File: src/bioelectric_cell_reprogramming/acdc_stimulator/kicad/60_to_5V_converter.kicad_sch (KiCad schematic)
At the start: 7 parts, among them IC5 LTC3637IMSE#PBF

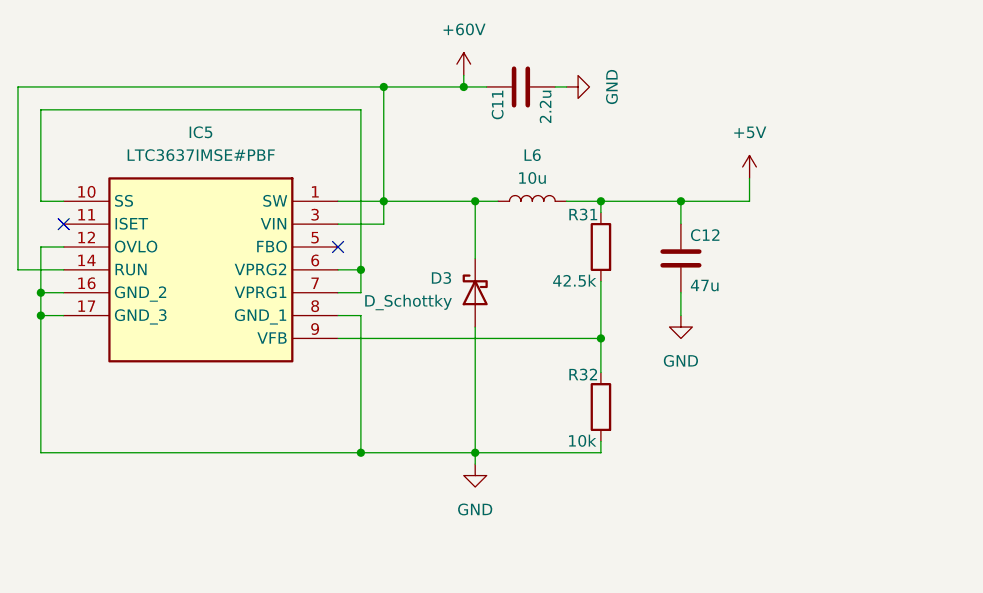
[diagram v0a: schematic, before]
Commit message: CI: footprint assignment done
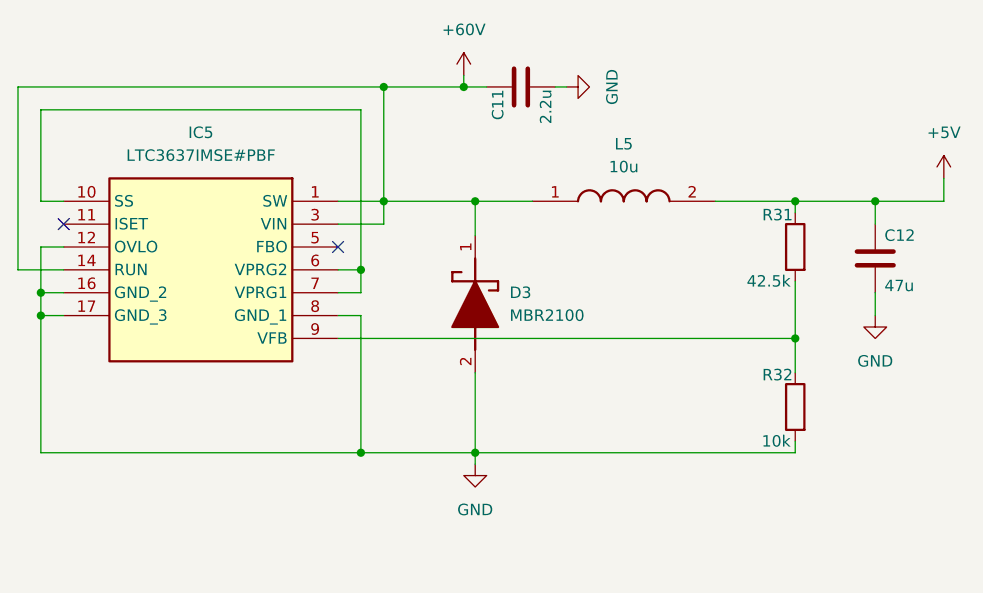
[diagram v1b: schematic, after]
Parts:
- removed D3: D_Schottky, symbol Device:D_Schottky
- removed L6: 10u, symbol Device:L
- added D3: MBR2100, MBR2100:DIOAD1910W86L670D310, symbol MBR2100:MBR2100
- added L5: 10u, SRP1270-100M:INDPM137137X700N, symbol SRP1270-100M:SRP1270-100M
- C11: footprint (none) -> Capacitor_SMD:C_0603_1608Metric
- C12: footprint (none) -> Capacitor_SMD:C_0805_2012Metric
- IC5: footprint LTC3637IMSEPBF -> LTC3637IMSE#PBF:LTC3637IMSEPBF
- R31, R32: footprint (none) -> Resistor_SMD:R_0402_1005Metric
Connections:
- net +5V: now also L5.2
- net +60V: now also D3.1 (K), L5.1
- net GND: now also D3.2 (A)
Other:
- moved on the sheet: C12, R31, R32

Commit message: ci: STM32 layout done and schematic annotated
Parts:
- renumbered C11 to C55, C12 to C56, L5 to L6, R31 to R30, R32 to R31
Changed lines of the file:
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@@
 		(dnp no)
 		(fields_autoplaced yes)
-		(property "Reference" "#PWR088"
+		(property "Reference" "#PWR093"
 			(at 219.71 86.36 0)
 			(effects
@@
 			(project "acdc_stimulator"
 				(path "/ec70e9f6-566f-44ea-8141-5580f51beca4/96d91c0a-dca3-4e1e-85a2-01b86266cb17"
-					(reference "#PWR088")
+					(reference "#PWR093")
 					(unit 1)
 				)
@@
 		(dnp no)
 		(fields_autoplaced yes)
-		(property "Reference" "#PWR087"
+		(property "Reference" "#PWR092"
 			(at 212.09 104.14 0)
 			(effects
@@
 			(project "acdc_stimulator"
 				(path "/ec70e9f6-566f-44ea-8141-5580f51beca4/96d91c0a-dca3-4e1e-85a2-01b86266cb17"
-					(reference "#PWR087")
+					(reference "#PWR092")
 					(unit 1)
 				)
@@
 		(on_board yes)
 		(dnp no)
-		(property "Reference" "C12"
+		(property "Reference" "C56"
 			(at 213.106 88.9 0)
 			(effects
@@
 			(project "acdc_stimulator"
 				(path "/ec70e9f6-566f-44ea-8141-5580f51beca4/96d91c0a-dca3-4e1e-85a2-01b86266cb17"
-					(reference "C12")
+					(reference "C56")
 					(unit 1)
 				)
@@
 		(dnp no)
 		(fields_autoplaced yes)
-		(property "Reference" "#PWR085"
+		(property "Reference" "#PWR090"
 			(at 167.64 120.65 0)
 			(effects
@@
 			(project "acdc_stimulator"
 				(path "/ec70e9f6-566f-44ea-8141-5580f51beca4/96d91c0a-dca3-4e1e-85a2-01b86266cb17"
-					(reference "#PWR085")
+					(reference "#PWR090")
 					(unit 1)
 				)
@@
 		(dnp no)
 		(fields_autoplaced yes)
-		(property "Reference" "#PWR084"
+		(property "Reference" "#PWR089"
 			(at 166.37 74.93 0)
 			(effects
@@
 			(project "acdc_stimulator"
 				(path "/ec70e9f6-566f-44ea-8141-5580f51beca4/96d91c0a-dca3-4e1e-85a2-01b86266cb17"
-					(reference "#PWR084")
+					(reference "#PWR089")
 					(unit 1)
 				)
@@
 		(dnp no)
 		(fields_autoplaced yes)
-		(property "Reference" "L5"
+		(property "Reference" "L6"
 			(at 184.15 78.74 0)
 			(effects
@@
 			(project ""
 				(path "/ec70e9f6-566f-44ea-8141-5580f51beca4/96d91c0a-dca3-4e1e-85a2-01b86266cb17"
-					(reference "L5")
+					(reference "L6")
 					(unit 1)
 				)
@@
 		(on_board yes)
 		(dnp no)
-		(property "Reference" "R32"
+		(property "Reference" "R31"
 			(at 202.946 104.394 0)
 			(effects
@@
 			(project "acdc_stimulator"
 				(path "/ec70e9f6-566f-44ea-8141-5580f51beca4/96d91c0a-dca3-4e1e-85a2-01b86266cb17"
-					(reference "R32")
+					(reference "R31")
 					(unit 1)
 				)
@@
 		(on_board yes)
 		(dnp no)
-		(property "Reference" "C11"
+		(property "Reference" "C55"
 			(at 170.18 72.644 0)
 			(effects
@@
 			(project "acdc_stimulator"
 				(path "/ec70e9f6-566f-44ea-8141-5580f51beca4/96d91c0a-dca3-4e1e-85a2-01b86266cb17"
-					(reference "C11")
+					(reference "C55")
 					(unit 1)
 				)
@@
 		(dnp no)
 		(fields_autoplaced yes)
-		(property "Reference" "#PWR086"
+		(property "Reference" "#PWR091"
 			(at 184.15 72.39 0)
 			(effects
@@
 			(project "acdc_stimulator"
 				(path "/ec70e9f6-566f-44ea-8141-5580f51beca4/96d91c0a-dca3-4e1e-85a2-01b86266cb17"
-					(reference "#PWR086")
+					(reference "#PWR091")
 					(unit 1)
 				)
@@
 		(on_board yes)
 		(dnp no)
-		(property "Reference" "R31"
+		(property "Reference" "R30"
 			(at 202.946 86.614 0)
 			(effects
@@
 			(project "acdc_stimulator"
 				(path "/ec70e9f6-566f-44ea-8141-5580f51beca4/96d91c0a-dca3-4e1e-85a2-01b86266cb17"
-					(reference "R31")
-					(unit 1)
-				)
+					(reference "R30")
+					(unit 1)
+				)

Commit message: ci: layout done
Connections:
- net +60V: no longer D3.1 (K), IC5.1 (SW), L6.1
- new net: D3.1 (K), IC5.1 (SW), L6.1
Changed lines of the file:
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@@
-	)
-	(junction
-		(at 157.48 85.09)
-		(diameter 0)
-		(color 0 0 0 0)
 	)
 	(junction
@@
 	)
 	(junction
+		(at 119.38 95.25)
+		(diameter 0)
+		(color 0 0 0 0)
+	)
+	(junction
+		(at 167.64 85.09)
+		(diameter 0)
+		(color 0 0 0 0)
+	)
+	(junction
+		(at 203.2 100.33)
+		(diameter 0)
+		(color 0 0 0 0)
+	)
+	(junction
 		(at 157.48 72.39)
-		(diameter 0)
-		(color 0 0 0 0)
-	)
-	(junction
-		(at 119.38 95.25)
-		(diameter 0)
-		(color 0 0 0 0)
-	)
-	(junction
-		(at 167.64 85.09)
-		(diameter 0)
-		(color 0 0 0 0)
-	)
-	(junction
-		(at 203.2 100.33)
 		(diameter 0)
 		(color 0 0 0 0)
@@
 	(wire
 		(pts
-			(xy 157.48 85.09) (xy 152.4 85.09)
+			(xy 152.4 85.09) (xy 167.64 85.09)
 		)
 		(stroke
@@
 	(wire
 		(pts
-			(xy 157.48 85.09) (xy 167.64 85.09)
-		)
-		(stroke
-			(width 0)
-			(type default)
-		)
-	)
-	(wire
-		(pts
 			(xy 154.94 92.71) (xy 154.94 95.25)
 		)
@@
 	(wire
 		(pts
-			(xy 157.48 72.39) (xy 157.48 85.09)
-		)
-		(stroke
-			(width 0)
-			(type default)
-		)
-	)
-	(wire
-		(pts
 			(xy 116.84 72.39) (xy 157.48 72.39)
 		)
@@
 	(wire
 		(pts
+			(xy 157.48 72.39) (xy 166.37 72.39)
+		)
+		(stroke
+			(width 0)
+			(type default)
+		)
+	)
+	(wire
+		(pts
 			(xy 203.2 111.76) (xy 203.2 113.03)
 		)
@@
 	(wire
 		(pts
-			(xy 166.37 72.39) (xy 157.48 72.39)
-		)
-		(stroke
-			(width 0)
-			(type default)
-		)
-	)
-	(wire
-		(pts
 			(xy 121.92 92.71) (xy 116.84 92.71)
 		)
@@
 	(wire
 		(pts
-			(xy 157.48 85.09) (xy 157.48 87.63)
-		)
-		(stroke
+			(xy 157.48 72.39) (xy 157.48 87.63)
+		)
+		(stroke

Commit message: fixed some more clearance errors
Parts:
- R31: Distributor Link (none) -> https://jlcpcb.com/partdetail/259901-NQ02WGJ0103TCE/C270371; Manufacturer (none) -> UNI-ROYAL(Uniroyal Elec); Manufacturer Part Number (none) -> NQ02WGJ0103TCE
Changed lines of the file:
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@@
+			)
+		)
+		(property "Distributor Link" ""
+			(at 167.64 86.36 0)
+			(effects
+				(font
+					(size 1.27 1.27)
+				)
+				(hide yes)
+			)
+		)
+		(property "Manufacturer" ""
+			(at 167.64 86.36 0)
+			(effects
+				(font
+					(size 1.27 1.27)
+				)
+				(hide yes)
+			)
+		)
+		(property "Manufacturer Part Number" ""
+			(at 167.64 86.36 0)
+			(effects
+				(font
+					(size 1.27 1.27)
+				)
+				(hide yes)
 			)
 		)
@@
 			)
 		)
+		(property "Distributor Link" ""
+			(at 152.4 85.09 0)
+			(effects
+				(font
+					(size 1.27 1.27)
+				)
+				(hide yes)
+			)
+		)
+		(property "Manufacturer" ""
+			(at 152.4 85.09 0)
+			(effects
+				(font
+					(size 1.27 1.27)
+				)
+				(hide yes)
+			)
+		)
+		(property "Manufacturer Part Number" ""
+			(at 152.4 85.09 0)
+			(effects
+				(font
+					(size 1.27 1.27)
+				)
+				(hide yes)
+			)
+		)
 		(pin "14"
 		)
@@
 		)
 		(property "Description" "Unpolarized capacitor"
+			(at 212.09 91.44 0)
+			(effects
+				(font
+					(size 1.27 1.27)
+				)
+				(hide yes)
+			)
+		)
+		(property "Distributor Link" ""
+			(at 212.09 91.44 0)
+			(effects
+				(font
+					(size 1.27 1.27)
+				)
+				(hide yes)
+			)
+		)
+		(property "Manufacturer" ""
+			(at 212.09 91.44 0)
+			(effects
+				(font
+					(size 1.27 1.27)
+				)
+				(hide yes)
+			)
+		)
+		(property "Manufacturer Part Number" ""
 			(at 212.09 91.44 0)
 			(effects
@@
 			)
 		)
+		(property "Distributor Link" ""
+			(at 173.99 85.09 0)
+			(effects
+				(font
+					(size 1.27 1.27)
+				)
+				(hide yes)
+			)
+		)
+		(property "Manufacturer" ""
+			(at 173.99 85.09 0)
+			(effects
+				(font
+					(size 1.27 1.27)
+				)
+				(hide yes)
+			)
+		)
+		(property "Manufacturer Part Number" ""
+			(at 173.99 85.09 0)
+			(effects
+				(font
+					(size 1.27 1.27)
+				)
+				(hide yes)
+			)
+		)
 		(pin "2"
 		)
@@
 			)
 		)
+		(property "Distributor Link" "https://jlcpcb.com/partdetail/259901-NQ02WGJ0103TCE/C270371"
+			(at 203.2 107.95 0)
+			(effects
+				(font
+					(size 1.27 1.27)
+				)
+				(hide yes)
+			)
+		)
+		(property "Manufacturer" "UNI-ROYAL(Uniroyal Elec)"
+			(at 203.2 107.95 0)
+			(effects
+				(font
+					(size 1.27 1.27)
+				)
+				(hide yes)
+			)
+		)
+		(property "Manufacturer Part Number" "NQ02WGJ0103TCE"
+			(at 203.2 107.95 0)
+			(effects
+				(font
+					(size 1.27 1.27)
+				)
+				(hide yes)
+			)
+		)
 		(pin "1"
 		)
@@
 		)
 		(property "Description" "Unpolarized capacitor"
+			(at 172.72 72.39 0)
+			(effects
+				(font
+					(size 1.27 1.27)
+				)
+				(hide yes)
+			)
+		)
+		(property "Distributor Link" ""
+			(at 172.72 72.39 0)
+			(effects
+				(font
+					(size 1.27 1.27)
+				)
+				(hide yes)
+			)
+		)
+		(property "Manufacturer" ""
+			(at 172.72 72.39 0)
+			(effects
+				(font
+					(size 1.27 1.27)
+				)
+				(hide yes)
+			)
+		)
+		(property "Manufacturer Part Number" ""
 			(at 172.72 72.39 0)
 			(effects
@@
 			(at 203.2 90.17 0)
 			(effects
+				(font
+					(size 1.27 1.27)
+				)
+				(hide yes)
+			)
+		)
+		(property "Distributor Link" ""
+			(at 203.2 90.17 0)
+			(effects
+				(font
+					(size 1.27 1.27)
+				)
+				(hide yes)
+			)
+		)
+		(property "Manufacturer" ""
+			(at 203.2 90.17 0)
+			(effects
+				(font
+					(size 1.27 1.27)
+				)
+				(hide yes)
+			)
+		)
+		(property "Manufacturer Part Number" ""
+			(at 203.2 90.17 0)
+			(effects

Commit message: BOM in progress
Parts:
- C55: Distributor Link (none) -> https://jlcpcb.com/partdetail/3409988-GRM21BD72A225KE01L/C2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; Manufacturer (none) -> Murata Electronics; Manufacturer Part Number (none) -> GRM21BD72A225KE01L
- C56: footprint Capacitor_SMD:C_0805_2012Metric -> Capacitor_SMD:C_1206_3216Metric; Distributor Link (none) -> https://jlcpcb.com/partdetail/183737-1206X476M160NT/C172351; Manufacturer (none) -> FH (Guangdong Fenghua Advanced Tech); Manufacturer Part Number (none) -> 1206X476M160NT
- D3: Distributor Link (none) -> https://www.digikey.com/en/products/detail/panjit-internati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; Manufacturer (none) -> Panjit International Inc.; Manufacturer Part Number (none) -> MBR2100_R2_00001
- IC5: Distributor Link (none) -> https://jlcpcb.com/partdetail/AnalogDevices-LTC3637IMSEPBF/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; Manufacturer (none) -> Analog Devices; Manufacturer Part Number (none) -> LTC3637IMSE#PBF
- L6: Distributor Link (none) -> https://www.mouser.com/ProductDetail/Bourns/SRP1270-100M?qs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; Manufacturer (none) -> Bourns; Manufacturer Part Number (none) -> SRP1270-100M
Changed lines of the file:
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@@
 			)
 		)
-		(property "Distributor Link" ""
+		(property "Distributor Link" "https://www.digikey.com/en/products/detail/panjit-international-inc/MBR2100-R2-00001/15801106"
 			(at 167.64 86.36 0)
 			(effects
@@
 			)
 		)
-		(property "Manufacturer" ""
+		(property "Manufacturer" "Panjit International Inc."
 			(at 167.64 86.36 0)
 			(effects
@@
 			)
 		)
-		(property "Manufacturer Part Number" ""
+		(property "Manufacturer Part Number" "MBR2100_R2_00001"
+			(at 167.64 86.36 0)
+			(effects
+				(font
+					(size 1.27 1.27)
+				)
+				(hide yes)
+			)
+		)
+		(property "JLCPCB Part #" ""
 			(at 167.64 86.36 0)
 			(effects
@@
 			)
 		)
-		(property "Distributor Link" ""
+		(property "Distributor Link" "https://jlcpcb.com/partdetail/AnalogDevices-LTC3637IMSEPBF/C580783"
 			(at 152.4 85.09 0)
 			(effects
@@
 			)
 		)
-		(property "Manufacturer" ""
+		(property "Manufacturer" "Analog Devices"
 			(at 152.4 85.09 0)
 			(effects
@@
 			)
 		)
-		(property "Manufacturer Part Number" ""
+		(property "Manufacturer Part Number" "LTC3637IMSE#PBF"
+			(at 152.4 85.09 0)
+			(effects
+				(font
+					(size 1.27 1.27)
+				)
+				(hide yes)
+			)
+		)
+		(property "JLCPCB Part #" ""
 			(at 152.4 85.09 0)
 			(effects
@@
 			)
 		)
-		(property "Footprint" "Capacitor_SMD:C_0805_2012Metric"
+		(property "Footprint" "Capacitor_SMD:C_1206_3216Metric"
 			(at 213.0552 95.25 0)
 			(effects
@@
 			)
 		)
-		(property "Distributor Link" ""
+		(property "Distributor Link" "https://jlcpcb.com/partdetail/183737-1206X476M160NT/C172351"
 			(at 212.09 91.44 0)
 			(effects
@@
 			)
 		)
-		(property "Manufacturer" ""
+		(property "Manufacturer" "FH (Guangdong Fenghua Advanced Tech)"
 			(at 212.09 91.44 0)
 			(effects
@@
 			)
 		)
-		(property "Manufacturer Part Number" ""
+		(property "Manufacturer Part Number" "1206X476M160NT"
+			(at 212.09 91.44 0)
+			(effects
+				(font
+					(size 1.27 1.27)
+				)
+				(hide yes)
+			)
+		)
+		(property "JLCPCB Part #" ""
 			(at 212.09 91.44 0)
 			(effects
@@
 			)
 		)
-		(property "Distributor Link" ""
+		(property "Distributor Link" "https://www.mouser.com/ProductDetail/Bourns/SRP1270-100M?qs=s%252BX%2FYkvGCpE5rFNaoMUDIw%3D%3D"
 			(at 173.99 85.09 0)
 			(effects
@@
 			)
 		)
-		(property "Manufacturer" ""
+		(property "Manufacturer" "Bourns"
 			(at 173.99 85.09 0)
 			(effects
@@
 			)
 		)
-		(property "Manufacturer Part Number" ""
+		(property "Manufacturer Part Number" "SRP1270-100M"
+			(at 173.99 85.09 0)
+			(effects
+				(font
+					(size 1.27 1.27)
+				)
+				(hide yes)
+			)
+		)
+		(property "JLCPCB Part #" ""
 			(at 173.99 85.09 0)
 			(effects
@@
 			)
 		)
+		(property "JLCPCB Part #" ""
+			(at 203.2 107.95 0)
+			(effects
+				(font
+					(size 1.27 1.27)
+				)
+				(hide yes)
+			)
+		)
 		(pin "1"
 		)
@@
 			)
 		)
-		(property "Distributor Link" ""
+		(property "Distributor Link" "https://jlcpcb.com/partdetail/3409988-GRM21BD72A225KE01L/C2981733"
 			(at 172.72 72.39 0)
 			(effects
@@
 			)
 		)
-		(property "Manufacturer" ""
+		(property "Manufacturer" " Murata Electronics"
 			(at 172.72 72.39 0)
 			(effects
@@
 			)
 		)
-		(property "Manufacturer Part Number" ""
+		(property "Manufacturer Part Number" "GRM21BD72A225KE01L"
+			(at 172.72 72.39 0)
+			(effects
+				(font
+					(size 1.27 1.27)
+				)
+				(hide yes)
+			)
+		)
+		(property "JLCPCB Part #" ""
 			(at 172.72 72.39 0)
 			(effects
@@
 			(at 203.2 90.17 0)
 			(effects
+				(font
+					(size 1.27 1.27)
+				)
+				(hide yes)
+			)
+		)
+		(property "JLCPCB Part #" ""
+			(at 203.2 90.17 0)
+			(effects

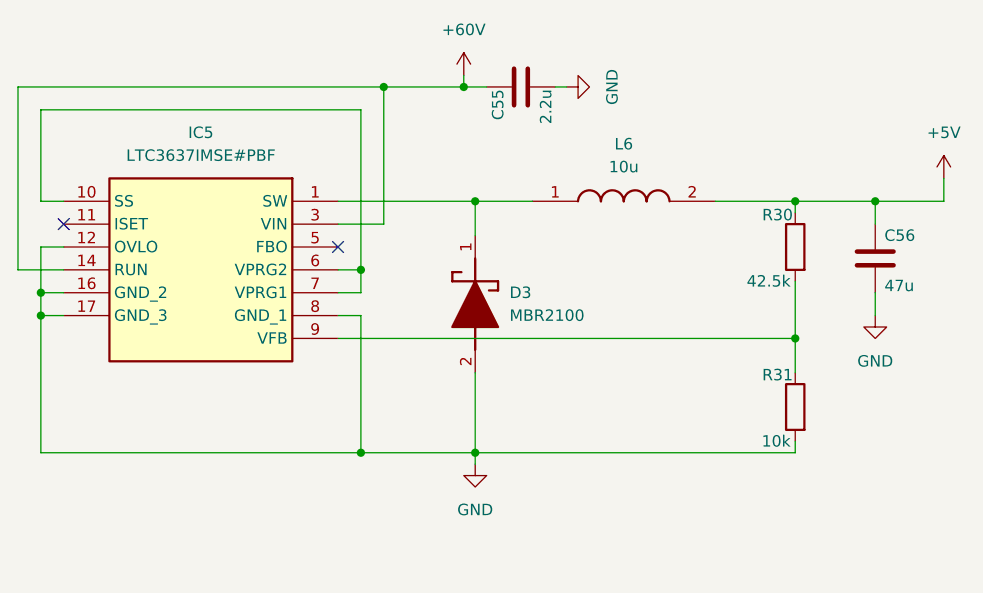
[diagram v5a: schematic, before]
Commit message: fixed values for resistive divider of LDOs
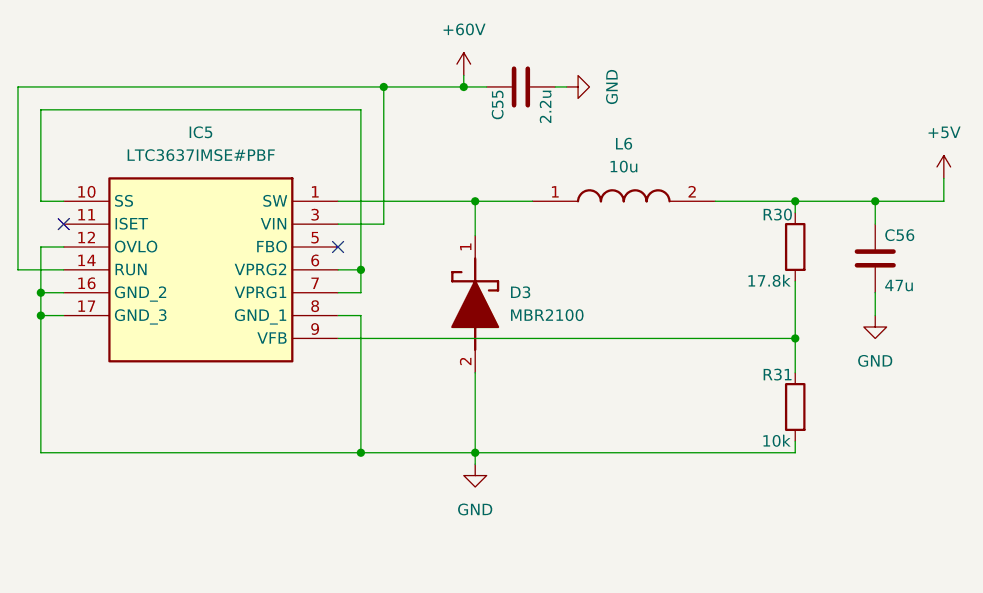
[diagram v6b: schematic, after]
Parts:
- L6: Distributor Link https://www.mouser.com/ProductDetail/Bourns/SRP1270-100M?qs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 -> https://jlcpcb.com/partdetail/Bourns-SRP1270100M/C2042024; Manufacturer Bourns -> BOURNS
- R30: value 42.5k -> 17.8k
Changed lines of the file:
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@@
 			)
 		)
-		(property "Distributor Link" "https://www.mouser.com/ProductDetail/Bourns/SRP1270-100M?qs=s%252BX%2FYkvGCpE5rFNaoMUDIw%3D%3D"
+		(property "Distributor Link" "https://jlcpcb.com/partdetail/Bourns-SRP1270100M/C2042024"
 			(at 173.99 85.09 0)
 			(effects
@@
 			)
 		)
-		(property "Manufacturer" "Bourns"
+		(property "Manufacturer" "BOURNS"
 			(at 173.99 85.09 0)
 			(effects
@@
 			)
 		)
-		(property "Value" "42.5k"
+		(property "Value" "17.8k"
 			(at 202.692 93.98 0)
 			(effects

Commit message: ci: BOM done
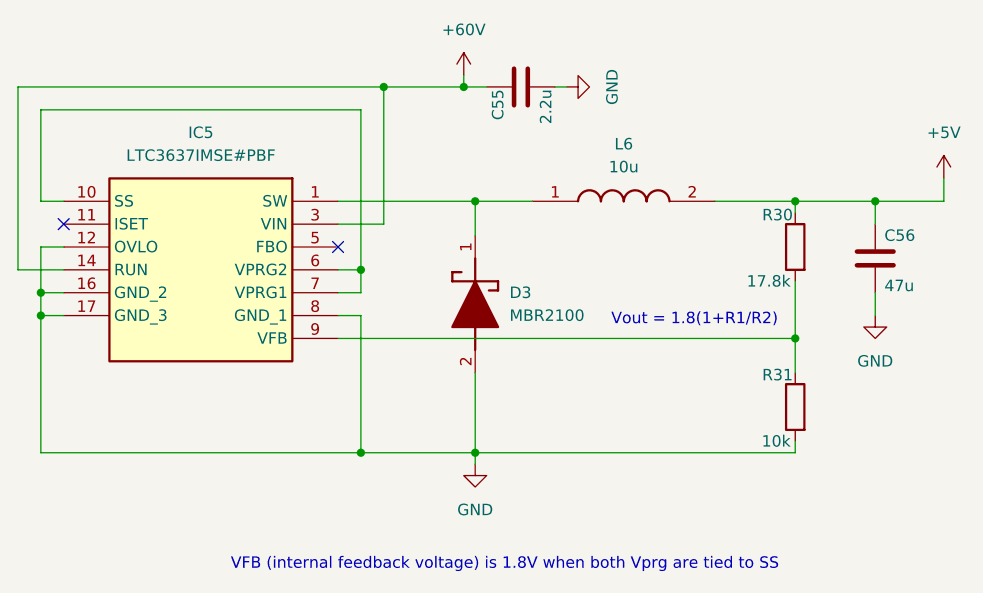
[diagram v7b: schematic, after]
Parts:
- R30: Distributor Link (none) -> https://jlcpcb.com/partdetail/Resi-PTFR0402B17K8N9/C2693055; Manufacturer (none) -> RESI; Manufacturer Part Number (none) -> PTFR0402B17K8N9
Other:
- note added: "VFB (internal feedback voltage) is 1.8V when both Vprg are tied to SS"
- note added: "Vout = 1.8(1+R1/R2)"
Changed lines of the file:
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@@
+		)
+	)
+	(text "VFB (internal feedback voltage) is 1.8V when both Vprg are tied to SS\n"
+		(exclude_from_sim no)
+		(at 170.942 125.476 0)
+		(effects
+			(font
+				(size 1.27 1.27)
+			)
+		)
+	)
+	(text "Vout = 1.8(1+R1/R2)"
+		(exclude_from_sim no)
+		(at 192.024 98.298 0)
+		(effects
+			(font
+				(size 1.27 1.27)
+			)
 		)
 	)
@@
 			)
 		)
-		(property "Distributor Link" ""
+		(property "Distributor Link" "https://jlcpcb.com/partdetail/Resi-PTFR0402B17K8N9/C2693055"
 			(at 203.2 90.17 0)
 			(effects
@@
 			)
 		)
-		(property "Manufacturer" ""
+		(property "Manufacturer" "RESI"
 			(at 203.2 90.17 0)
 			(effects
@@
 			)
 		)
-		(property "Manufacturer Part Number" ""
+		(property "Manufacturer Part Number" "PTFR0402B17K8N9"
 			(at 203.2 90.17 0)
 			(effects

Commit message: ci: build files for v0.0.2 generated
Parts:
- removed D3: MBR2100, MBR2100:DIOAD1910W86L670D310, symbol MBR2100:MBR2100
- removed L6: 10u, SRP1270-100M:INDPM137137X700N, symbol SRP1270-100M:SRP1270-100M
- added D2: B2100AE-13, DIOM5226X240N, symbol B2100AE-13:B2100AE-13
- added L5: 10u, INDPM8080X420N, symbol SWPA8040S100MT:SWPA8040S100MT
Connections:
- net +5V: now also L5.2
- net GND: now also D2.2 (A)
- net at IC5.1 (SW): now also D2.1 (K), L5.1
